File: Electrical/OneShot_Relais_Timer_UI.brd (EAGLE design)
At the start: 57.3 x 60.4 mm, 13 parts, among them IC1 4511D

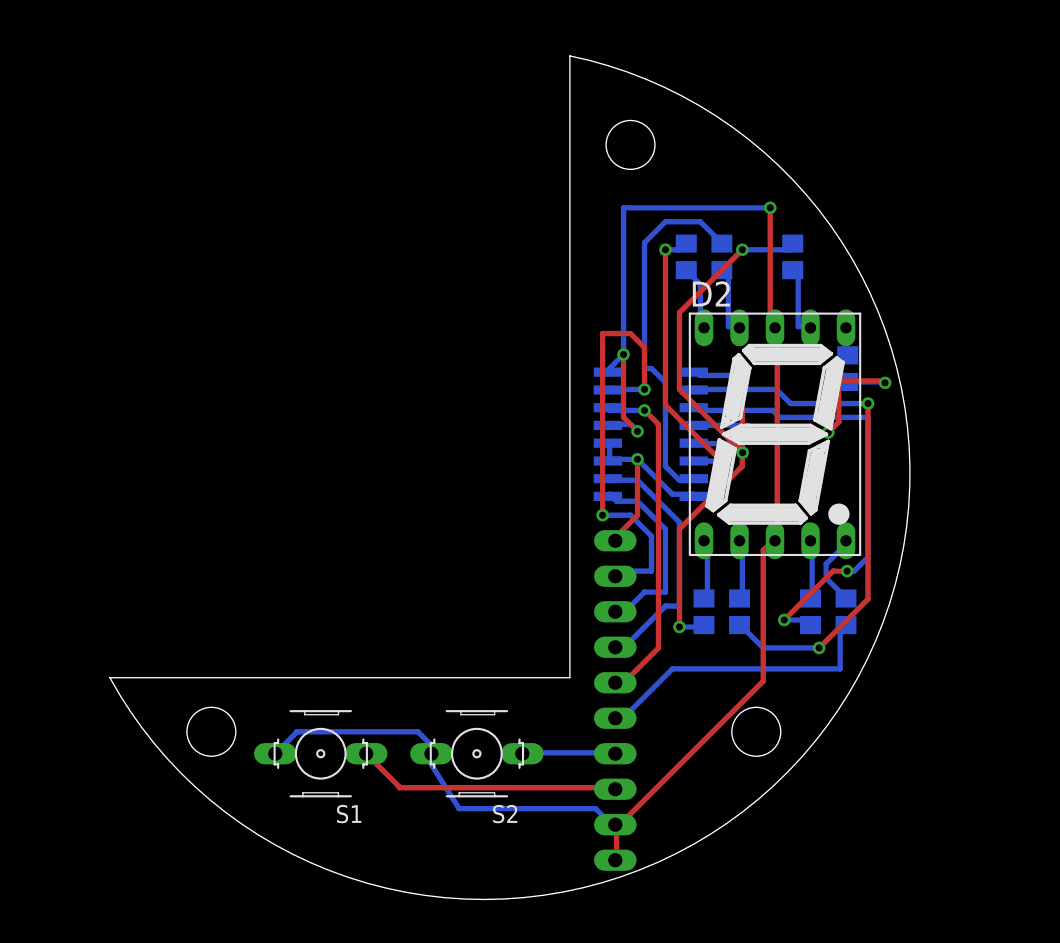
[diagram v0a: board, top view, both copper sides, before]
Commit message: Added mounting holes to PCB, moved relay, small adaptions to UI PCB
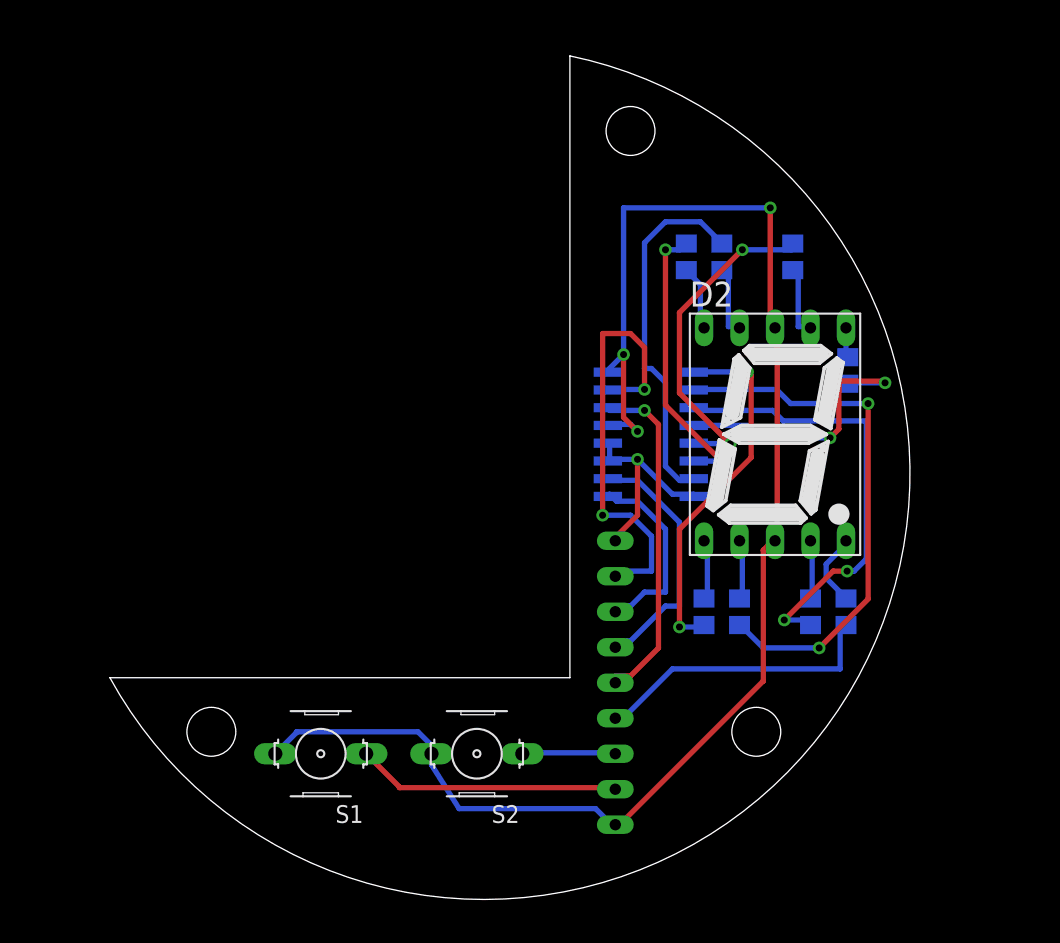
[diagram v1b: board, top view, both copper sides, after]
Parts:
- JP1: device pinhead:1X10 -> OwnDevices:FE09
- moved JP1 1.27 mm to (41.9, 16.5)
- moved R4 0.13 mm to (58.5, 38.9)
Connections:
- net GND: no longer JP1.10
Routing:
- net GND: track 112.0 -> 109.4 mm
- net N$4: track 26.0 -> 23.8 mm
- net N$8: track 25.2 -> 26.1 mm
- net N$5: track 19.9 -> 20.5 mm

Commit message: Added GND planes, refined routing
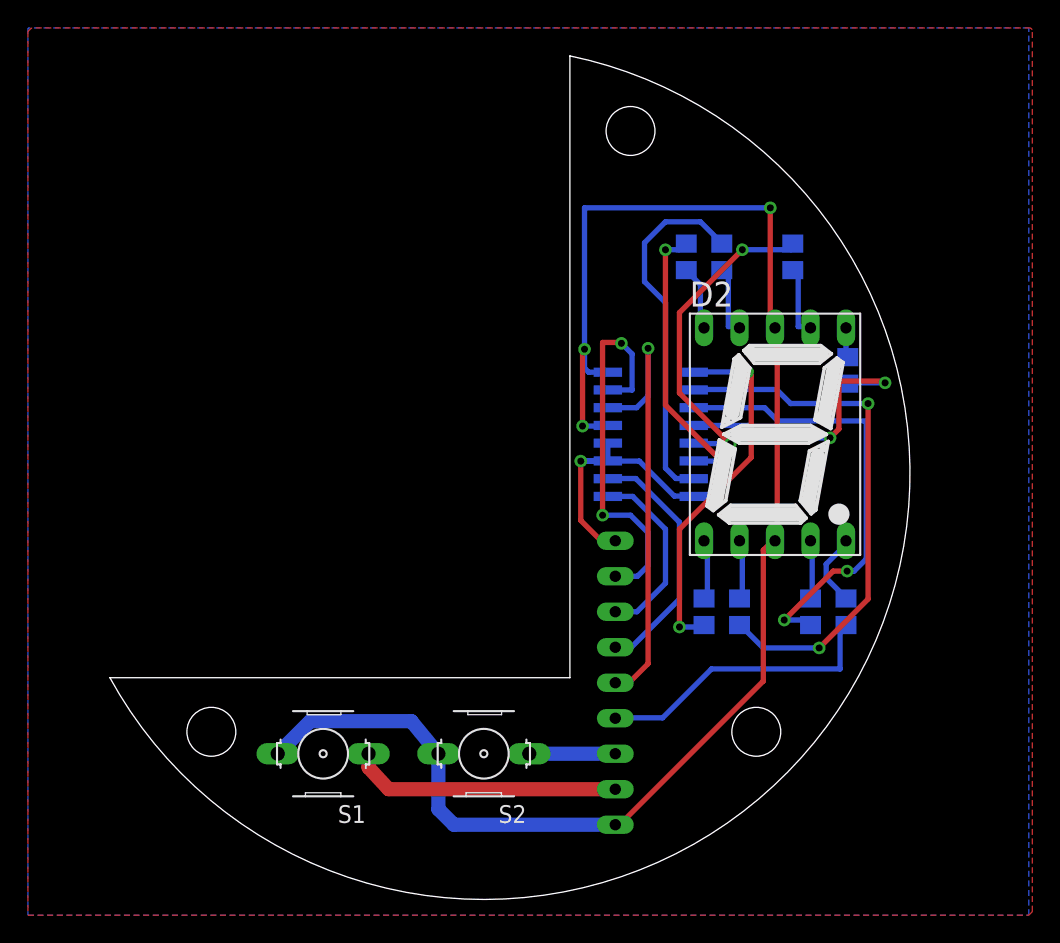
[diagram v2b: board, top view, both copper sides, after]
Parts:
- moved S2 0.50 mm to (32.5, 11.4)
- moved S1 0.17 mm to (21.0, 11.4)
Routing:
- net BCD_7SEG_4: track 24.5 -> 32.1 mm
- net +5V: track 15.0 -> 20.7 mm
- net GND: track 109.4 -> 114.1 mm
- net BCD_7SEG_1: track 31.6 -> 27.9 mm
- net BCD_7SEG_2: track 14.1 -> 13.4 mm
- net BTN_START_STOP: track 6.72 -> 6.16 mm
- net BCD_7SEG_3: track 18.5 -> 17.9 mm
- added copper zone on layer 1, net GND
- added copper zone on layer 16, net GND

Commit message: Moved 12V regulator to other side, improved texts, improved UI PCB (increased vias and traces)
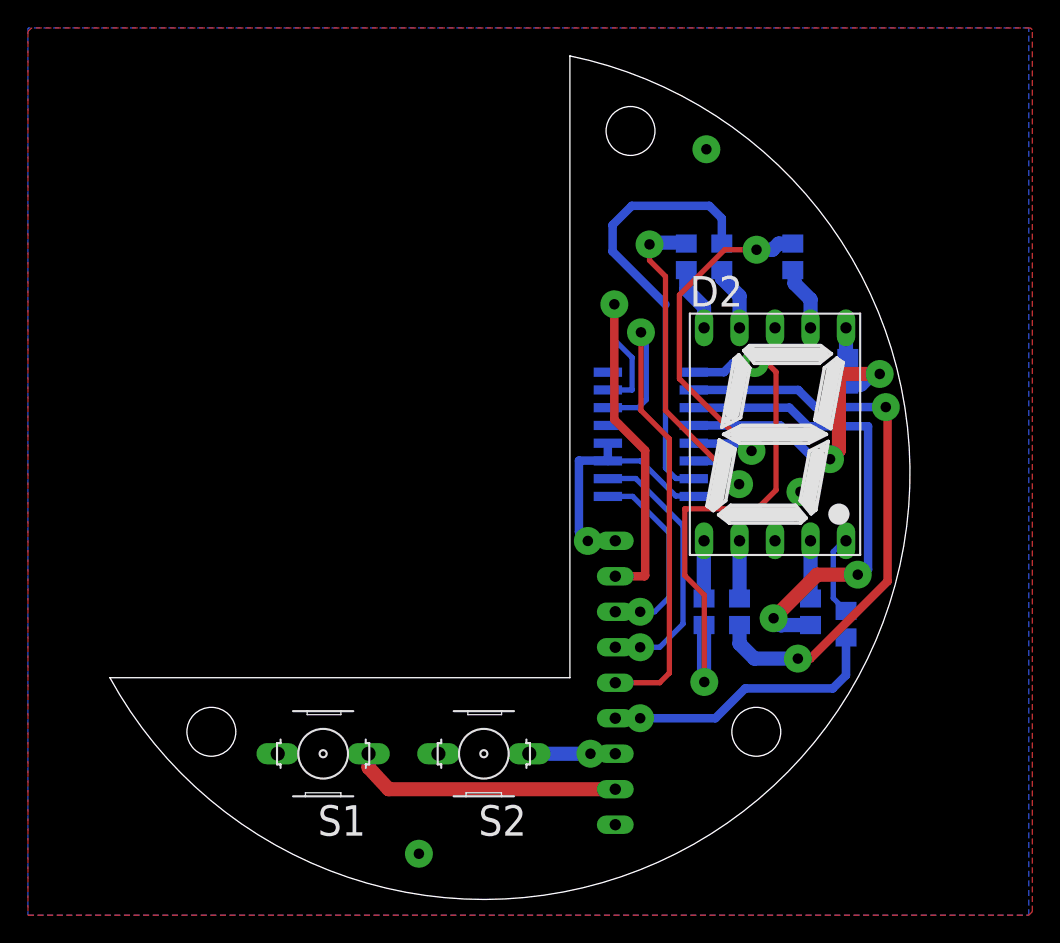
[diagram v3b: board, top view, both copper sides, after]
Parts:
- moved R10 0.89 mm to (58.4, 20.7)
- moved R4 0.06 mm to (58.5, 38.8)
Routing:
- net GND: track 114.1 -> 0.00 mm
- net N$8: track 26.1 -> 39.0 mm
- net N$10: track 20.4 -> 26.5 mm
- net N$9: track 25.9 -> 31.9 mm
- net BCD_7SEG_4: track 32.1 -> 37.4 mm
- net N$4: track 23.8 -> 27.3 mm
- net N$7: track 38.2 -> 41.4 mm
- net BCD_7SEG_1: track 27.9 -> 30.9 mm, vias 2 -> 1
- net N$5: track 20.5 -> 22.6 mm
- net N$6: track 32.3 -> 34.3 mm
- net BCD_7SEG_3: track 17.9 -> 19.3 mm, vias 0 -> 1
- net +5V: track 20.7 -> 19.6 mm
- net BCD_7SEG_2: track 13.4 -> 14.4 mm, vias 0 -> 1
- net N$16: track 5.28 -> 4.66 mm
- net N$11: track 5.28 -> 4.66 mm
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
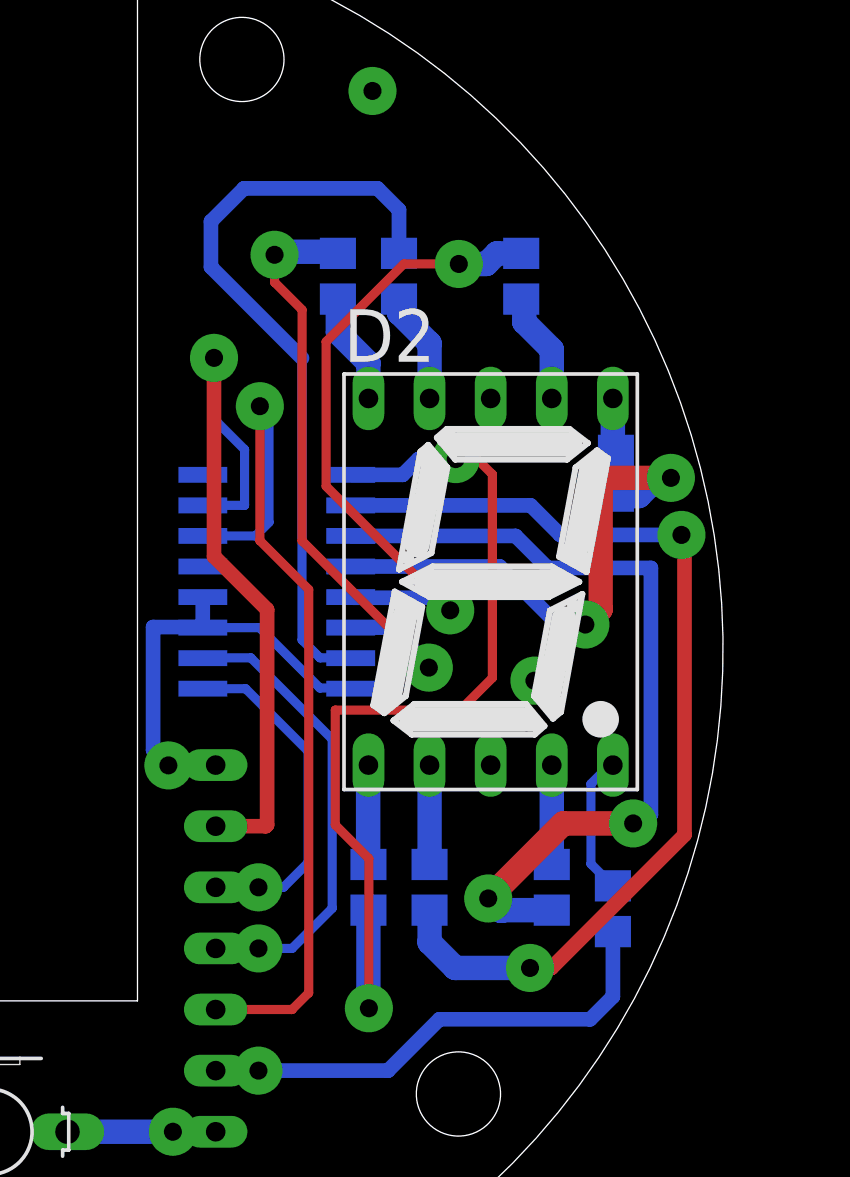
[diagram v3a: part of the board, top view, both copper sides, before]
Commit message: Replaced BCD 7Segment IC with correct type (footprint), corrected routing of UI PCB
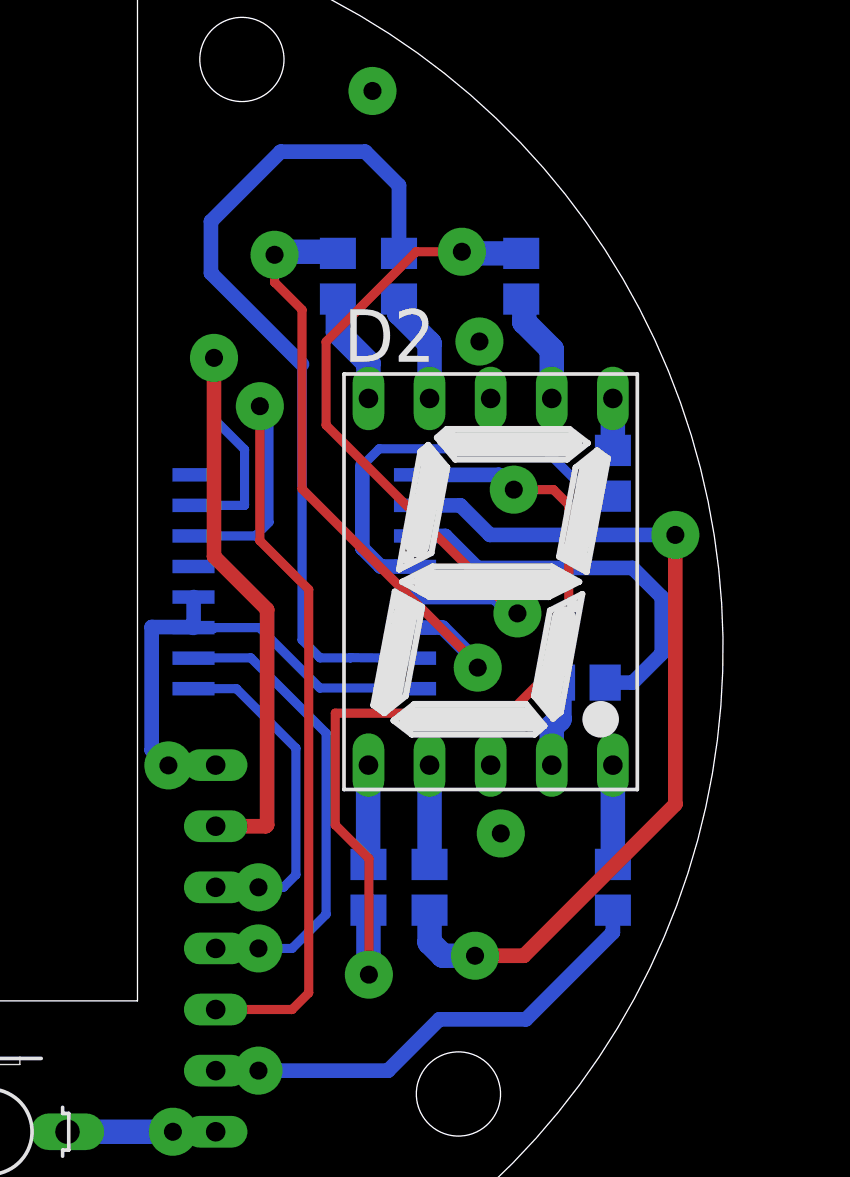
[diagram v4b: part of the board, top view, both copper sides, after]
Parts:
- IC1: value 4511D -> 4511; device 45xx:SO16 -> OwnDevices:SOIC127P1032X265-16L
- moved R5 8.60 mm to (57.1, 30.1), turned to 0 degrees
- moved IC1 1.14 mm to (45.6, 34.3), turned to 180 degrees
- moved R10 0.89 mm to (58.4, 21.6)
- moved R4 0.13 mm to (58.4, 38.8)
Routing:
- net N$6: track 34.3 -> 16.5 mm, vias 2 -> 0
- net N$5: track 22.6 -> 17.5 mm, vias 2 -> 0
- net N$9: track 31.9 -> 36.4 mm
- net N$7: track 41.4 -> 36.9 mm
- net +5V: track 19.6 -> 23.1 mm
- net N$19: track 5.85 -> 4.13 mm
- net N$4: track 27.3 -> 28.9 mm
- net N$8: track 39.0 -> 38.0 mm
- net BCD_7SEG_DOT: track 20.5 -> 19.8 mm
- net N$13: track 4.13 -> 3.56 mm

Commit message: Small adaptions to PCBs, schematics, and mechanical components
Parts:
- R10, R3, R4, R5, R6, R7, R8, R9: value 150 -> 330
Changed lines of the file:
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@@
 <attribute name="VALUE" x="24.048" y="16.51" size="1.27" layer="27" ratio="10" rot="R180"/>
 </element>
-<element name="R3" library="OwnDevices" library_urn="urn:adsk.eagle:library:19498084" package="R0805" package3d_urn="urn:adsk.eagle:package:23553/2" value="150" x="54.61" y="46.99" smashed="yes" rot="MR270">
+<element name="R3" library="OwnDevices" library_urn="urn:adsk.eagle:library:19498084" package="R0805" package3d_urn="urn:adsk.eagle:package:23553/2" value="330" x="54.61" y="46.99" smashed="yes" rot="MR270">
 <attribute name="NAME" x="57.404" y="48.133" size="1.6764" layer="26" ratio="15" rot="MR270"/>
 <attribute name="POPULARITY" value="86" x="54.61" y="46.99" size="1.778" layer="28" rot="MR270" display="off"/>
@@
 <attribute name="VALUE" x="57.15" y="47.625" size="1.27" layer="28" rot="MR270"/>
 </element>
-<element name="R4" library="OwnDevices" library_urn="urn:adsk.eagle:library:19498084" package="R0805" package3d_urn="urn:adsk.eagle:package:23553/2" value="150" x="58.42" y="38.8" smashed="yes" rot="MR90">
+<element name="R4" library="OwnDevices" library_urn="urn:adsk.eagle:library:19498084" package="R0805" package3d_urn="urn:adsk.eagle:package:23553/2" value="330" x="58.42" y="38.8" smashed="yes" rot="MR90">
 <attribute name="NAME" x="59.563" y="37.784" size="1.6764" layer="26" ratio="15" rot="MR90"/>
 <attribute name="POPULARITY" value="86" x="58.42" y="38.8" size="1.778" layer="28" rot="MR90" display="off"/>
@@
 <attribute name="VALUE" x="55.88" y="38.165" size="1.27" layer="28" rot="MR90"/>
 </element>
-<element name="R5" library="OwnDevices" library_urn="urn:adsk.eagle:library:19498084" package="R0805" package3d_urn="urn:adsk.eagle:package:23553/2" value="150" x="57.15" y="30.099" smashed="yes" rot="MR0">
+<element name="R5" library="OwnDevices" library_urn="urn:adsk.eagle:library:19498084" package="R0805" package3d_urn="urn:adsk.eagle:package:23553/2" value="330" x="57.15" y="30.099" smashed="yes" rot="MR0">
 <attribute name="NAME" x="56.515" y="32.766" size="1.6764" layer="26" ratio="15" rot="MR180"/>
 <attribute name="POPULARITY" value="86" x="57.15" y="30.099" size="1.778" layer="28" rot="MR0" display="off"/>
@@
 <attribute name="VALUE" x="57.785" y="27.559" size="1.27" layer="28" rot="MR0"/>
 </element>
-<element name="R6" library="OwnDevices" library_urn="urn:adsk.eagle:library:19498084" package="R0805" package3d_urn="urn:adsk.eagle:package:23553/2" value="150" x="50.8" y="21.59" smashed="yes" rot="MR90">
+<element name="R6" library="OwnDevices" library_urn="urn:adsk.eagle:library:19498084" package="R0805" package3d_urn="urn:adsk.eagle:package:23553/2" value="330" x="50.8" y="21.59" smashed="yes" rot="MR90">
 <attribute name="NAME" x="52.197" y="20.32" size="1.6764" layer="26" ratio="15" rot="MR90"/>
 <attribute name="POPULARITY" value="86" x="50.8" y="21.59" size="1.778" layer="28" rot="MR90" display="off"/>
@@
 <attribute name="VALUE" x="48.26" y="20.955" size="1.27" layer="28" rot="MR90"/>
 </element>
-<element name="R7" library="OwnDevices" library_urn="urn:adsk.eagle:library:19498084" package="R0805" package3d_urn="urn:adsk.eagle:package:23553/2" value="150" x="48.26" y="21.59" smashed="yes" rot="MR90">
+<element name="R7" library="OwnDevices" library_urn="urn:adsk.eagle:library:19498084" package="R0805" package3d_urn="urn:adsk.eagle:package:23553/2" value="330" x="48.26" y="21.59" smashed="yes" rot="MR90">
 <attribute name="NAME" x="45.466" y="20.066" size="1.6764" layer="26" ratio="15" rot="MR90"/>
 <attribute name="POPULARITY" value="86" x="48.26" y="21.59" size="1.778" layer="28" rot="MR90" display="off"/>
@@
 <attribute name="VALUE" x="45.72" y="20.955" size="1.27" layer="28" rot="MR90"/>
 </element>
-<element name="R8" library="OwnDevices" library_urn="urn:adsk.eagle:library:19498084" package="R0805" package3d_urn="urn:adsk.eagle:package:23553/2" value="150" x="49.53" y="46.99" smashed="yes" rot="MR270">
+<element name="R8" library="OwnDevices" library_urn="urn:adsk.eagle:library:19498084" package="R0805" package3d_urn="urn:adsk.eagle:package:23553/2" value="330" x="49.53" y="46.99" smashed="yes" rot="MR270">
 <attribute name="NAME" x="50.419" y="51.816" size="1.6764" layer="26" ratio="15" rot="MR270"/>
 <attribute name="POPULARITY" value="86" x="49.53" y="46.99" size="1.778" layer="28" rot="MR270" display="off"/>
@@
 <attribute name="VALUE" x="52.07" y="47.625" size="1.27" layer="28" rot="MR270"/>
 </element>
-<element name="R9" library="OwnDevices" library_urn="urn:adsk.eagle:library:19498084" package="R0805" package3d_urn="urn:adsk.eagle:package:23553/2" value="150" x="46.99" y="46.99" smashed="yes" rot="MR270">
+<element name="R9" library="OwnDevices" library_urn="urn:adsk.eagle:library:19498084" package="R0805" package3d_urn="urn:adsk.eagle:package:23553/2" value="330" x="46.99" y="46.99" smashed="yes" rot="MR270">
 <attribute name="NAME" x="48.006" y="51.816" size="1.6764" layer="26" ratio="15" rot="MR270"/>
 <attribute name="POPULARITY" value="86" x="46.99" y="46.99" size="1.778" layer="28" rot="MR270" display="off"/>
@@
 <attribute name="VALUE" x="47.244" y="23.368" size="1.778" layer="27" ratio="10"/>
 </element>
-<element name="R10" library="OwnDevices" library_urn="urn:adsk.eagle:library:19498084" package="R0805" package3d_urn="urn:adsk.eagle:package:23553/2" value="150" x="58.42" y="21.59" smashed="yes" rot="MR270">
+<element name="R10" library="OwnDevices" library_urn="urn:adsk.eagle:library:19498084" package="R0805" package3d_urn="urn:adsk.eagle:package:23553/2" value="330" x="58.42" y="21.59" smashed="yes" rot="MR270">
 <attribute name="NAME" x="57.15" y="23.622" size="1.6764" layer="26" ratio="15" rot="MR270"/>
 <attribute name="POPULARITY" value="86" x="58.42" y="21.59" size="1.778" layer="28" rot="MR270" display="off"/>
